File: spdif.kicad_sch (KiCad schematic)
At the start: 2 parts, among them U13 DIR9001PWR, U5 DIR9001PWR

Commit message: asd
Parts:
- removed U13, U5: DIR9001PWR, User:PW28, symbol User:DIR9001PWR
- added C73, C74, C75, C76, C77, C78, C79, C80: 1uF, PCM_JLCPCB:C_0402, symbol PCM_JLCPCB-Capacitors:0402,1uF
- added C88, C89, C90, C91, C92, C93: 100nF, PCM_JLCPCB:C_0402, symbol PCM_JLCPCB-Capacitors:0402,100nF
- added D10, D9: BAT54WS, PCM_JLCPCB:D_SOD-323, symbol PCM_JLCPCB-Diodes:Schottky,BAT54WS
- added J1: Footswitch_1, symbol Connector_Generic:Conn_01x02
- added J12: Footswitch_2, symbol Connector_Generic:Conn_01x02
- added J13: Switch_1, symbol Connector_Generic:Conn_01x03
- added J14: Switch_2, symbol Connector_Generic:Conn_01x03
- added Q3: BC846BS, Package_TO_SOT_SMD:SOT-363_SC-70-6, symbol Transistor_BJT:BC846BS
- added Q4: BC856BS, Package_TO_SOT_SMD:SOT-363_SC-70-6, symbol Transistor_BJT:BC856BS
- added R2, R4: 1MΩ, PCM_JLCPCB:R_0402, symbol PCM_JLCPCB-Resistors:0402,1MΩ
- added R30, R35: 120Ω, PCM_JLCPCB:R_0402, symbol PCM_JLCPCB-Resistors:0402,120Ω
- added R40, R45, R74, R78, R84, R85, R86, R87, R92, R93, R94, R95, R96, R97: 10kΩ, PCM_JLCPCB:R_0402, symbol PCM_JLCPCB-Resistors:0402,10kΩ
- added R5: 2kΩ, PCM_JLCPCB:R_0402, symbol PCM_JLCPCB-Resistors:0402,2kΩ
- added RV1, RV2, RV3, RV4, RV5, RV6: 10k, symbol Device:R_Potentiometer
- added U15: ISOM8115, Package_SO:SOIC-4_4.55x2.6mm_P1.27mm, symbol Isolator:EL814
- added U7: 74HC14, symbol 74xx:74HC14
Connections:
- new net: J1.1 (Pin_1), R74.2, R78.1
- new net: C88.1, R78.2, U7.1
- new net: C92.1, R96.2, U7.11
- new net: Q3.2 (B1), Q3.3 (C2), R45.2
- new net: Q3.1 (E1), Q3.5 (B2), R30.1
- new net: J12.1 (Pin_1), R84.2, R85.1
- new net: C93.1, R97.2, U7.13
- new net: J13.1 (Pin_1), R86.2, R87.1
- new net: J13.3 (Pin_3), R92.2, R93.1
- new net: C91.1, R93.2, U7.9
- new net: J14.3 (Pin_3), R95.2, R97.1
- new net: Q4.1 (E1), Q4.5 (B2), R35.2
- new net: Q4.2 (B1), Q4.3 (C2), R40.1
- new net: D9.2, Q4.6 (C1)
- new net: J14.1 (Pin_1), R94.2, R96.1
- new net: C90.1, R87.2, U7.5
- new net: D10.1, Q3.6 (C1)
- new net: C89.1, R85.2, U7.3
- new net +2.5VA: RV1.1, RV2.1, RV3.1, RV4.1, RV5.1, RV6.1
- new net +3.3V: Q4.4 (E2), R35.1, R5.1, R74.1, R84.1, R86.1, R92.1, R94.1, R95.1, U7.14 (VCC)
- new net Footswitch_1: U7.2
- new net Footswitch_2: U7.4
- new net GND: C73.2, C74.2, C75.2, C76.2, C77.2, C78.2, C79.2, C80.2, C88.2, C89.2, C90.2, C91.2, C92.2, C93.2, J1.2 (Pin_2), J12.2 (Pin_2), J13.2 (Pin_2), J14.2 (Pin_2), Q3.4 (E2), R2.2, R30.2, R4.2, R40.2, RV1.3, RV2.3, RV3.3, RV4.3, RV5.3, RV6.3, U7.7 (GND)
- new net GNDPWR: U15.3
- new net MIDI IN Shield: C73.1, C74.1, C75.1, C76.1, R2.1
- new net MIDI OUT Shield: C77.1, C78.1, C79.1, C80.1, R4.1
- new net MIDI Out Sink: D10.2
- new net MIDI Out Source: D9.1
- new net Midi In Sink: U15.2
- new net Midi In Source: U15.1
- new net Potentiometer_1: RV1.2
- new net Potentiometer_2: RV2.2
- new net Potentiometer_3: RV3.2
- new net Potentiometer_4: RV4.2
- new net Potentiometer_5: RV5.2
- new net Potentiometer_6: RV6.2
- new net Switch_1A: U7.6
- new net Switch_1B: U7.8
- new net Switch_2A: U7.10
- new net Switch_2B: U7.12
- new net UART0_RX: R5.2, U15.4
- new net UART0_TX: R45.1
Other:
- note added: "?"
- note added: "MIDI"

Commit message: added decoupling for DSP
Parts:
- added C100, C101, C102, C103, C104, C105, C97, C98, C99: 100nF, PCM_JLCPCB:C_0402, symbol PCM_JLCPCB-Capacitors:0402,100nF
- added R104, R105, R106, R107, R108, R109: 100Ω, PCM_JLCPCB:R_0402, symbol PCM_JLCPCB-Resistors:0402,100Ω
- added R110, R111, R112, R113, R114, R115: 10kΩ, PCM_JLCPCB:R_0402, symbol PCM_JLCPCB-Resistors:0402,10kΩ
- added U25, U26: TLV9004xRUCR, Package_DFN_QFN:Texas_S-PX2QFN-14, symbol Amplifier_Operational:TLV9004xRUCR
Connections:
- net +3.3V: now also C99.1
- net GND: now also C100.2, C101.2, C102.2, C103.2, C104.2, C105.2, C97.2, C98.2, C99.2, U25.10 (V-), U26.10 (V-)
- net Potentiometer_1: now also R104.2; no longer RV1.2
- net Potentiometer_2: now also R105.2; no longer RV2.2
- net Potentiometer_3: now also R106.2; no longer RV3.2
- net Potentiometer_4: now also R107.2; no longer RV4.2
- net Potentiometer_5: now also R108.2; no longer RV5.2
- net Potentiometer_6: now also R109.2; no longer RV6.2
- new net: C105.1, R115.2, U26.4 (+)
- new net: U26.12 (-), U26.13
- new net: C101.1, R111.2, U25.4 (+)
- new net: R105.1, U25.5 (-), U25.6
- new net: R108.1, U26.1 (-), U26.14
- new net: C104.1, R114.2, U26.2 (+)
- new net: R104.1, U25.1 (-), U25.14
- new net: R112.1, RV3.2
- new net: C102.1, R112.2, U25.9 (+)
- new net: U26.7, U26.8 (-)
- new net: R106.1, U25.7, U25.8 (-)
- new net: R110.1, RV1.2
- new net: R107.1, U25.12 (-), U25.13
- new net: C100.1, R110.2, U25.2 (+)
- new net: R114.1, RV5.2
- new net: R113.1, RV4.2
- new net: R111.1, RV2.2
- new net: R109.1, U26.5 (-), U26.6
- new net: C103.1, R113.2, U25.11 (+)
- new net: R115.1, RV6.2
- new net +3.3VA2: C97.1, C98.1, U25.3 (V+), U26.3 (V+)
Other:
- moved on the sheet: C88, C89, C90, C91, C92, C93, J1, J12, J13, J14, R74, R78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

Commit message: commit
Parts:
- removed C74, C75, C76, C77, C78, C79, C80: 1uF, PCM_JLCPCB:C_0402, symbol PCM_JLCPCB-Capacitors:0402,1uF
- removed D10, D9: BAT54WS, PCM_JLCPCB:D_SOD-323, symbol PCM_JLCPCB-Diodes:Schottky,BAT54WS
- removed Q3: BC846BS, Package_TO_SOT_SMD:SOT-363_SC-70-6, symbol Transistor_BJT:BC846BS
- removed Q4: BC856BS, Package_TO_SOT_SMD:SOT-363_SC-70-6, symbol Transistor_BJT:BC856BS
- removed R2, R4: 1MΩ, PCM_JLCPCB:R_0402, symbol PCM_JLCPCB-Resistors:0402,1MΩ
- removed R30, R35: 120Ω, PCM_JLCPCB:R_0402, symbol PCM_JLCPCB-Resistors:0402,120Ω
- removed R40, R45: 10kΩ, PCM_JLCPCB:R_0402, symbol PCM_JLCPCB-Resistors:0402,10kΩ
- added D2: SMF6.0CA, PCM_JLCPCB:D_SOD-123FL, symbol PCM_JLCPCB-Diodes:TVS-Bi,SMF6.0CA
- added R2: 220Ω, PCM_JLCPCB:R_0805, symbol PCM_JLCPCB-Resistors:0805,220Ω
- added R30, R4: 100kΩ, PCM_JLCPCB:R_0402, symbol PCM_JLCPCB-Resistors:0402,100kΩ
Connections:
- net +3.3VA2: now also R4.1
- net GND: now also D2.1, R30.2
- net MIDI IN Shield: now also D2.2
- net Midi In Sink: now also R2.1; no longer U15.2
- net +3.3VA2_Midpoint: now reaches U26.11 (+)
- net +3.3VA2_Midpoint: now also U26.9 (+), R30.1, R4.2
- new net: R2.2, U15.2
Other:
- note removed: "?"
- moved on the sheet: C97, C98, R104, R105, R106, R5, U15, U25E, U26C, U26D, U26E

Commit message: lot of changes
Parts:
- removed C73: 1uF, PCM_JLCPCB:C_0402, symbol PCM_JLCPCB-Capacitors:0402,1uF
- removed C97, C98: 100nF, PCM_JLCPCB:C_0402, symbol PCM_JLCPCB-Capacitors:0402,100nF
- removed D2: SMF6.0CA, PCM_JLCPCB:D_SOD-123FL, symbol PCM_JLCPCB-Diodes:TVS-Bi,SMF6.0CA
- removed R104, R105, R106, R107, R108, R109: 100Ω, PCM_JLCPCB:R_0402, symbol PCM_JLCPCB-Resistors:0402,100Ω
- removed R110, R111, R112, R113, R114, R115: 10kΩ, PCM_JLCPCB:R_0402, symbol PCM_JLCPCB-Resistors:0402,10kΩ
- removed R2: 220Ω, PCM_JLCPCB:R_0805, symbol PCM_JLCPCB-Resistors:0805,220Ω
- removed R30, R4: 100kΩ, PCM_JLCPCB:R_0402, symbol PCM_JLCPCB-Resistors:0402,100kΩ
- removed R5: 2kΩ, PCM_JLCPCB:R_0402, symbol PCM_JLCPCB-Resistors:0402,2kΩ
- removed U15: ISOM8115, Package_SO:SOIC-4_4.55x2.6mm_P1.27mm, symbol Isolator:EL814
- removed U25, U26: TLV9004xRUCR, Package_DFN_QFN:Texas_S-PX2QFN-14, symbol Amplifier_Operational:TLV9004xRUCR
- added R30, R37, R38, R4, R41, R42: 1kΩ, PCM_JLCPCB:R_0402, symbol PCM_JLCPCB-Resistors:0402,1kΩ
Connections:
- net Potentiometer_1: now also C100.1, R4.2
- net Potentiometer_2: now also C101.1, R30.2
- net Potentiometer_3: now also C102.1, R37.2
- net Potentiometer_4: now also C103.1, R38.2
- net Potentiometer_5: now also C104.1, R41.2
- net Potentiometer_6: now also C105.1, R42.2
- net at RV3.2: now also R37.1
- net at RV1.2: now also R4.1
- net at RV5.2: now also R41.1
- net at RV4.2: now also R38.1
- net at RV2.2: now also R30.1
- net at RV6.2: now also R42.1
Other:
- note removed: "MIDI"
- moved on the sheet: C88, C89, C90, C91, C92, C93, C99, J1, J12, J13, J14, R74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

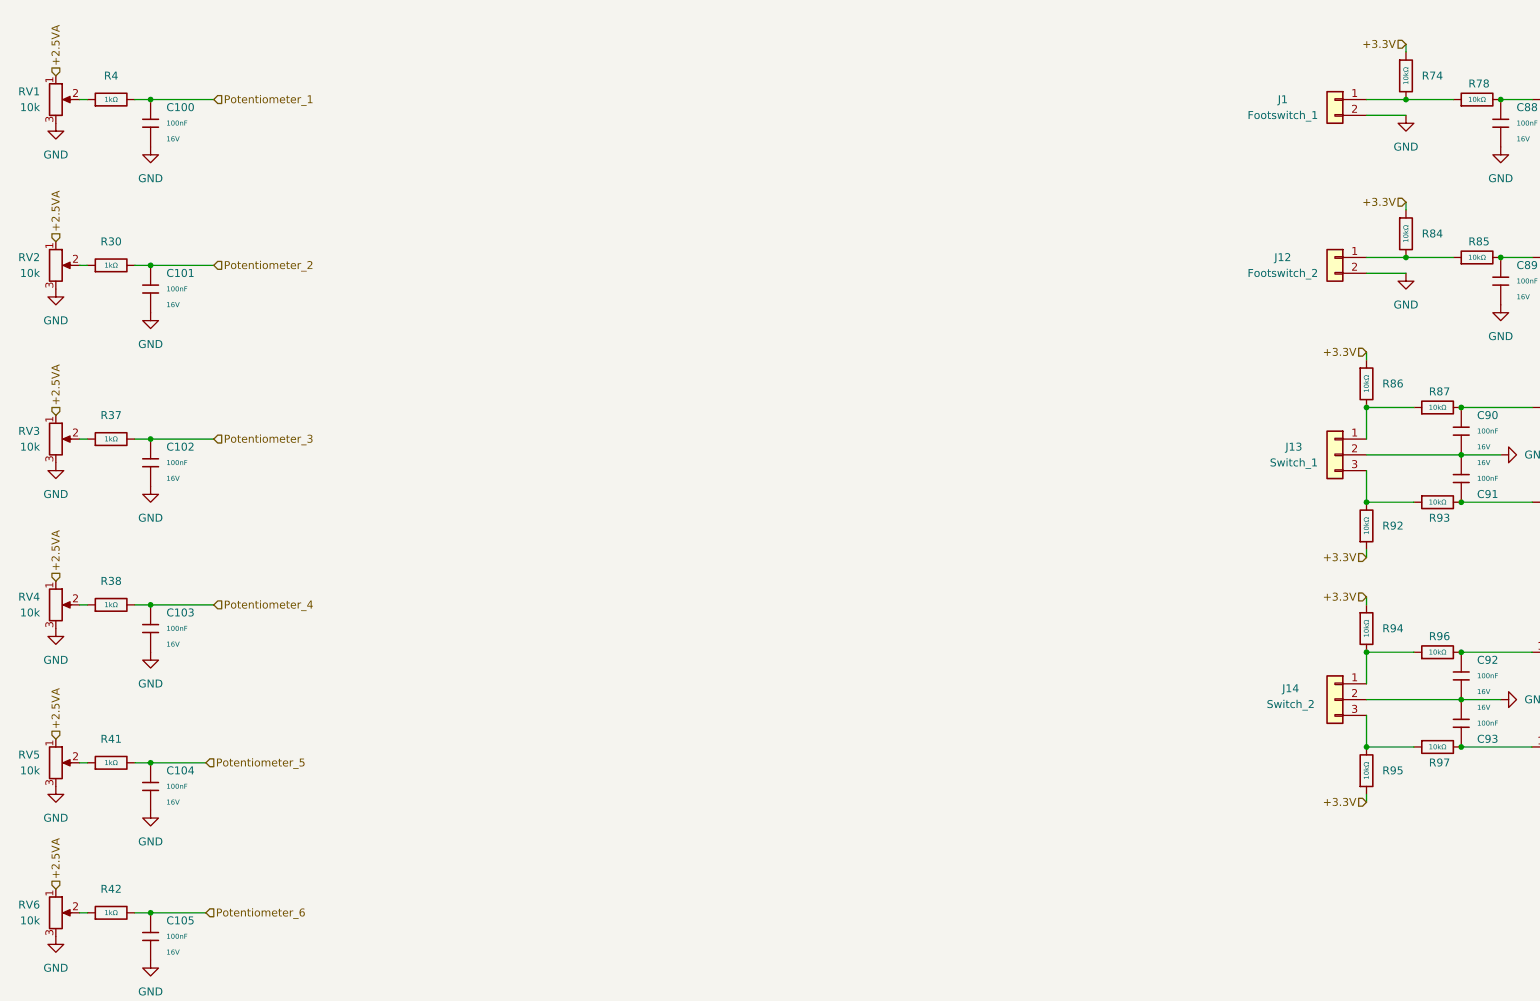
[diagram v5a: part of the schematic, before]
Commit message: imrt1176 is added
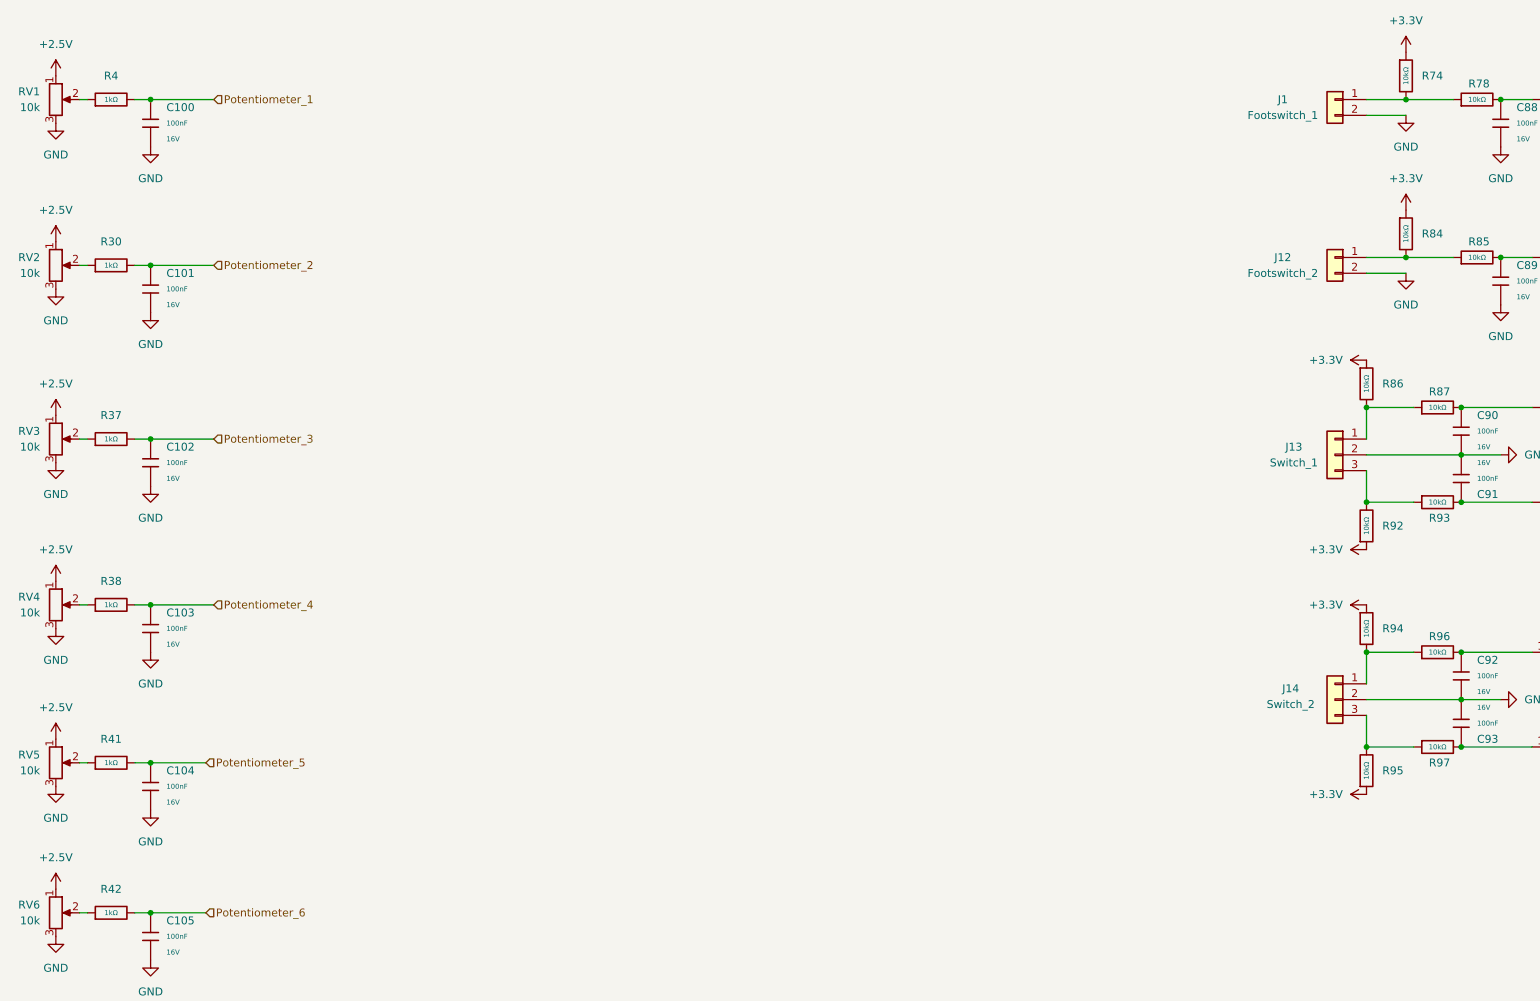
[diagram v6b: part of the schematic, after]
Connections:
- net +2.5VA renamed +2.5V
